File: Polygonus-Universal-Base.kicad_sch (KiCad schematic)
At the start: 6 parts, among them J4 Polygonus_Plugs, J5 Conn_02x04_Top_Bottom, U1 WBO-Single-Module

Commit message: Made the board
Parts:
- removed JP1: Jumper_2_Open, Resistor_THT:R_Axial_DIN0309_L9.0mm_D3.2mm_P15.24mm_Horizontal, symbol Jumper:Jumper_2_Open
- J4: footprint Simon:Polygonus_Plugs -> Simon:Polygonus-With-USB-SWD
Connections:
- net LSU_12v is gone; now on net 12V_MR_FUSE: J5.1 (Pin_1), J5.2 (Pin_2)
- net 12V_KEY: now also Motronic_88pin1.21
- net 12V_MR: now also Motronic_88pin1.10, Motronic_88pin1.28, Motronic_88pin1.37, Motronic_88pin1.68
- net 12V_MR_FUSE: no longer Motronic_88pin1.28
- net 5V_SENSOR_1: now also Motronic_88pin1.58, Motronic_88pin1.59
- net 5V_SENSOR_2: now also Motronic_88pin1.56, Motronic_88pin1.57
- net AT1: now also Motronic_88pin1.15
- net AT2: now also Motronic_88pin1.73
- net AT3: now also Motronic_88pin1.43
- net AT4: now also Motronic_88pin1.16
- net AV1: now also Motronic_88pin1.38
- net AV10: now also Motronic_88pin1.72
- net AV11: now also Motronic_88pin1.14
- net AV2: now also Motronic_88pin1.11
- net AV3: now also Motronic_88pin1.69
- net AV4: now also Motronic_88pin1.39
- net AV5: now also Motronic_88pin1.12
- net AV6: now also Motronic_88pin1.70
- net AV7: now also Motronic_88pin1.40
- net AV8: now also Motronic_88pin1.13
- net AV9: now also Motronic_88pin1.71
- net CAN+: now also Motronic_88pin1.75
- net CAN-: now also Motronic_88pin1.74
- net CRANK +: now also Motronic_88pin1.41
- net CRANK -: now also Motronic_88pin1.42
- net DIGITAL_1: now also Motronic_88pin1.65
- net DIGITAL_2: now also Motronic_88pin1.64
- net DIGITAL_3: now also Motronic_88pin1.63
- net DIGITAL_4: now also Motronic_88pin1.62
- net DIGITAL_5: now also Motronic_88pin1.61
- net DIGITAL_6: now also Motronic_88pin1.60
- net ETB1_+: now also Motronic_88pin1.34
- net ETB1_-: now also Motronic_88pin1.6
- net ETB2_+: now also Motronic_88pin1.33
- net ETB2_-: now also Motronic_88pin1.5
- net ExtraLSA: now also Motronic_88pin1.1
- net ExtraLSB: now also Motronic_88pin1.29
- net ExtraLSC: now also Motronic_88pin1.2
- net ExtraLSD: now also Motronic_88pin1.30
- net GND: now also Motronic_88pin1.55
- net HS1: now also Motronic_88pin1.32
- net HS2: now also Motronic_88pin1.4
- net HS3: now also Motronic_88pin1.31
- net HS4: now also Motronic_88pin1.3
- net IGBT1: now also Motronic_88pin1.25
- net IGBT2: now also Motronic_88pin1.52
- net IGBT3: now also Motronic_88pin1.24
- net IGBT4: now also Motronic_88pin1.51
- net IGBT5: now also Motronic_88pin1.23
- net IGBT6: now also Motronic_88pin1.50
- net IGBT7: now also Motronic_88pin1.22
- net IGBT8: now also Motronic_88pin1.49
- net KNOCK_1: now also Motronic_88pin1.35
- net KNOCK_2: now also Motronic_88pin1.7
- net LS1: now also Motronic_88pin1.76
- net LS10ADD: now also Motronic_88pin1.26
- net LS11ADD: now also Motronic_88pin1.54
- net LS12ADD: now also Motronic_88pin1.27
- net LS13: now also Motronic_88pin1.88
- net LS14: now also Motronic_88pin1.87
- net LS15: now also Motronic_88pin1.86
- net LS16: now also Motronic_88pin1.85
- net LS2: now also Motronic_88pin1.77
- net LS3: now also Motronic_88pin1.78
- net LS4: now also Motronic_88pin1.79
- net LS5: now also Motronic_88pin1.80
- net LS6: now also Motronic_88pin1.81
- net LS7: now also Motronic_88pin1.82
- net LS8: now also Motronic_88pin1.83
- net LS9ADD: now also Motronic_88pin1.53
- net Perm_Live: now also Motronic_88pin1.84

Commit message: Competed board
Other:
- note removed: "1 Fuel pump 2 ICV close 3 inj 1 4 inj 4 5 inj 6 6 GND injection 7 inj 7 8 check engine 9 10 11 transmisson TPS 12 HEGO signal 13 HEGO signal 14 MAF ground 15 Injection signal resistor? 16 CPS pos 17 Cam sensor 18 19 Secondary air pump 20 21 22 IGN 7 23 IGN 6 24 IGN 4 25 IGN 1 26 12v B+junction 27 Main relay 28 GND shields and sensors"
- note removed: "1 Fuel pump 2 ICV close 3 inj 5 4 inj 6 5 inj 4 6 GND injection 7 vanos 8 check engine 9 10 11 transmisson TPS 12 13 HEGO signal 14 MAF ground 15 GND via resistor? 16 CPS pos 17 Cam sensor 18 19 20 21 22 23 IGN 4 24 IGN 6 25 IGN 5 26 12v B+junction 27 Main relay 28 GND shields and sensors"
- note removed: "29 ICV open 30 31 inj 3 32 inj 2 33 inj 1 34 GND 35 36 EVAP 37 38 HEGO heater 39 40 HEGO signal gnd 41 MAF 42 VSS 43 CPS neg 44 GND sensors 45 GND shields 46 TI fuel 47 Tacho 48 AC control 49 50 ign 1 51 ign 2 52 ign 3 53 54 Main relay voltage 55 GND ignition"
- note removed: "29 ICV open 30 31 inj 3 32 inj 2 33 inj 1 34 GND 35 inj 2 36 EVAP 37 HEGO heater 38 39 HEGO signal gnd 40 HEGO signal gnd 41 MAF signal 42 VSS 43 CPS neg 44 GND sensors 45 GND shields 46 TI fuel 47 Tacho 48 AC control 49 IGN 2 50 IGN 3 51 IGN 8 52 IGN 5 53 54 Main relay voltage 55 GND ignition"
- note removed: "56 12v key 57 58 59 5v sensor 60 data link 61 62 EML abs/asc 63 64 AC switch 65 AC pressure 66 EWSII 67 Knock 68 Knock 69 Knock 70 Knock 71 GND knock sensor 72 73 TPS 74 75 76 77 IAT 78 ECT 79 80 81 Headlights on signal 82 Engine overrun signal ABS/ASC 83 traction regulation ABS/ASC 84 GND 85 TCU data 86 TCU data 87 RxD 88 TxD"
- note removed: "56 12v key 57 Transmission IGN RET 58 59 5v sensor 60 data link 61 62 EML abs/asc 63 64 AC switch 65 AC pressure 66 EWSII 67 68 69 Knock 70 Knock 71 GND knock sensor 72 73 TPS 74 75 76 77 IAT 78 ECT 79 80 81 Trans range switch 82 Throttle ABS/ASC 83 Ignition ABS/ASC 84 85 86 87 RxD 88 TxD"
- note removed: "Large Pins 1 to 6 22 to 28 29 to 34 49 to 55"
- moved on the sheet: F1, J4, J5, Motronic_88pin1A, U1

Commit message: upgraded
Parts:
- added C10: 1u, Resistor_SMD:R_0805_2012Metric, symbol hellen-one-common:Res
- added C11: 56u, Capacitor_THT:CP_Radial_D8.0mm_P3.50mm, symbol Device:CP
- added J1: Conn_02x04_Top_Bottom, Connector_Molex:Molex_Micro-Fit_3.0_43045-0800_2x04_P3.00mm_Horizontal, symbol Connector_Generic:Conn_02x04_Top_Bottom
- added R13, R14: DNP, Resistor_SMD:R_0805_2012Metric, symbol hellen-one-common:Res
- added U14: WBO-Single-Module, wideband_module:f042_wideband_module, symbol Simon:WBO-Single-Module
- J4: footprint Simon:Polygonus-With-USB-SWD -> Simon:Polygonus_Plugs; symbol Simon:Polygonus_Plugs -> Simon:Polygonus-With-USB-SWD
- U1: footprint Simon:f042_wideband_module -> wideband_module:f042_wideband_module
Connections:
- net +5V: now also U14.1 (5v_in)
- net 12V_MR: no longer Motronic_88pin1.10, Motronic_88pin1.37, Motronic_88pin1.68
- net 12V_MR_FUSE: now also Motronic_88pin1.10, Motronic_88pin1.37, Motronic_88pin1.68, C11.1, J1.1 (Pin_1), J1.2 (Pin_2)
- net 5V_SENSOR_1: no longer J4.39 (Pin_39)
- net 5V_SENSOR_2: no longer J4.38 (Pin_38)
- net CAN2+: no longer U1.5 (CANRX)
- net CAN2-: no longer U1.6 (CANTX)
- net GND: now also C10.2, C11.2, U14.10 (GND), U14.2 (GND), U14.3 (Select1), U14.9 (GND)
- net RC1: now reaches J4.75 (Pin_75)
- net RC1: now also R13.2
- net RC2: now reaches J4.76 (Pin_76)
- net RC2: now also R14.2
- new net: C10.1, R13.1, R14.1
- new net CAN_RX: U1.5 (CANRX)
- new net CAN_RX2: U14.5 (CANRX)
- new net CAN_TX: U1.6 (CANTX)
- new net CAN_TX2: U14.6 (CANTX)
- new net HeaterNeg2: J1.5 (Pin_5), J1.6 (Pin_6), U14.11 (HeaterNeg), U14.12 (HeaterNeg)
- new net LSU_Ip2: J1.3 (Pin_3), U14.13 (LSU_Ip)
- new net LSU_Rtrim2: J1.8 (Pin_8), U14.15 (LSU_Rtrim)
- new net LSU_Un2: J1.4 (Pin_4), U14.16 (LSU_Un)
- new net LSU_Vm2: J1.7 (Pin_7), U14.14 (LSU_Vm)
- no-connect marks 8 -> 11
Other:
- added sheet WBO-CAN-TRANS (wbo-can-trans.kicad_sch)
- added sheet WBO-CAN-TRANS1 (wbo-can-trans.kicad_sch)

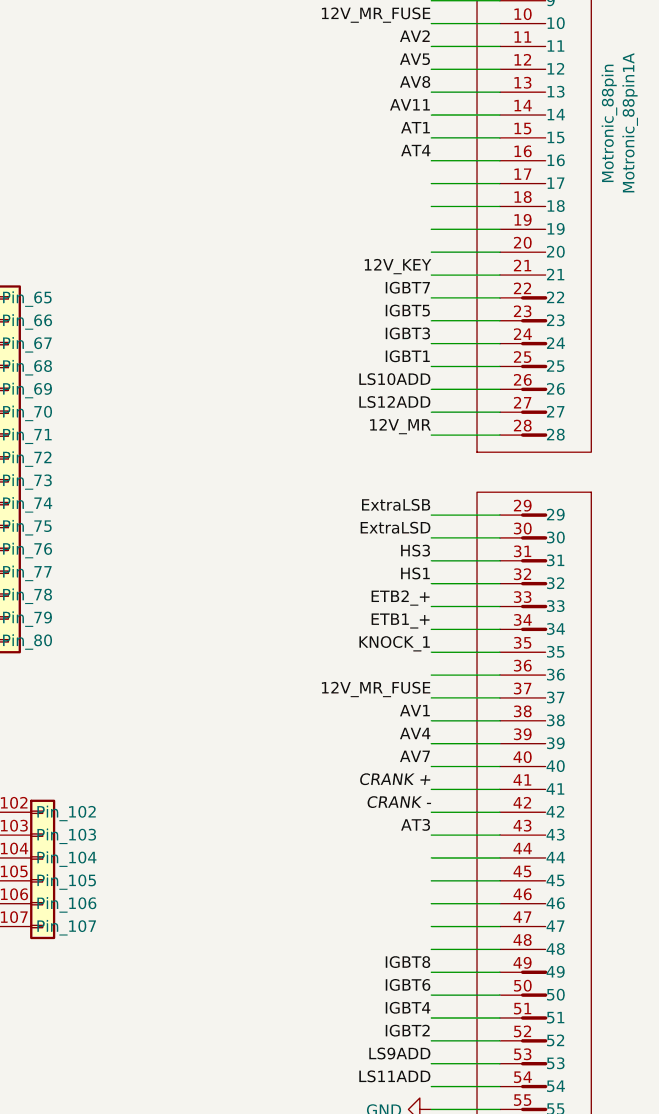
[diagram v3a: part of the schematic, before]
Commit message: Modified IGBTs and routed smart coils
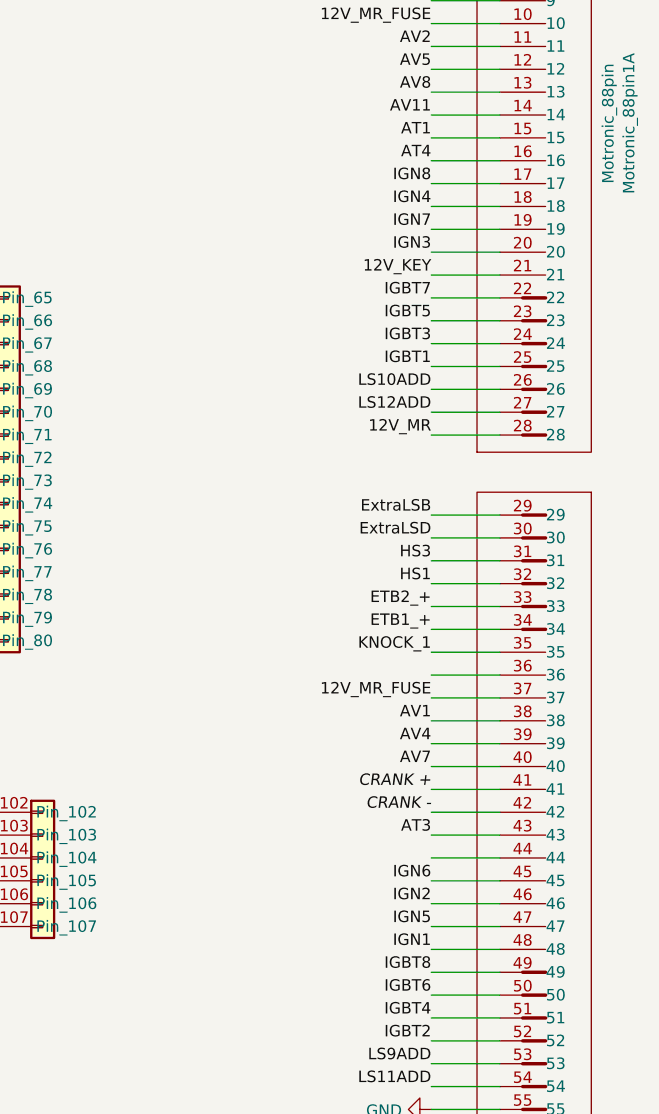
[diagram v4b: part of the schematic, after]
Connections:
- net IGN1: now also Motronic_88pin1.48
- net IGN2: now also Motronic_88pin1.46
- net IGN3: now also Motronic_88pin1.20
- net IGN4: now also Motronic_88pin1.18
- net IGN5: now also Motronic_88pin1.47
- net IGN6: now also Motronic_88pin1.45
- net IGN7: now also Motronic_88pin1.19
- net IGN8: now also Motronic_88pin1.17
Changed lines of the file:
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@@
+    (effects (font (size 1.27 1.27)) (justify right bottom))
+  )
+  (label "IGN4" (at 271.78 73.66 180)
     (effects (font (size 1.27 1.27)) (justify right bottom))
   )
@@
     (effects (font (size 1.27 1.27)) (justify right bottom))
   )
+  (label "IGN6" (at 271.78 148.59 180)
+    (effects (font (size 1.27 1.27)) (justify right bottom))
+  )
   (label "5V_SENSOR_2" (at 271.78 181.61 180)
     (effects (font (size 1.27 1.27)) (justify right bottom))
@@
   )
   (label "12V_MR_FUSE" (at 271.78 53.34 180)
+    (effects (font (size 1.27 1.27)) (justify right bottom))
+  )
+  (label "IGN1" (at 271.78 156.21 180)
     (effects (font (size 1.27 1.27)) (justify right bottom))
   )
@@
     (effects (font (size 1.27 1.27)) (justify right bottom))
   )
+  (label "IGN3" (at 271.78 78.74 180)
+    (effects (font (size 1.27 1.27)) (justify right bottom))
+  )
   (label "12V_MR_FUSE" (at 153.0898 220.274 0)
     (effects (font (size 1.27 1.27)) (justify left bottom))
@@
     (effects (font (size 1.27 1.27)) (justify right bottom))
   )
+  (label "IGN8" (at 271.78 71.12 180)
+    (effects (font (size 1.27 1.27)) (justify right bottom))
+  )
   (label "KNOCK_1" (at 168.91 161.29 180)
     (effects (font (size 1.27 1.27)) (justify right bottom))
@@
     (effects (font (size 1.27 1.27)) (justify right bottom))
   )
+  (label "IGN2" (at 271.78 151.13 180)
+    (effects (font (size 1.27 1.27)) (justify right bottom))
+  )
   (label "AV7" (at 168.91 143.51 180)
     (effects (font (size 1.27 1.27)) (justify right bottom))
@@
     (effects (font (size 1.27 1.27)) (justify right bottom))
   )
+  (label "IGN5" (at 271.78 153.67 180)
+    (effects (font (size 1.27 1.27)) (justify right bottom))
+  )
   (label "IGN7" (at 149.86 46.99 180)
     (effects (font (size 1.27 1.27)) (justify right bottom))
@@
     (effects (font (size 1.27 1.27)) (justify right bottom))
   )
+  (label "IGN7" (at 271.78 76.2 180)
+    (effects (font (size 1.27 1.27)) (justify right bottom))
+  )

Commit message: updated and fixed, check JLC exports
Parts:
- J4: footprint Simon:Polygonus_Plugs -> Simon:Polygonus-With-USB-SWD
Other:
- moved on the sheet: C10, C11, F1, J1, J5, R13, R14, U1, U14

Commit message: All fixed up for JLC
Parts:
- C10, R13, R14: LCSC C23241 -> DNP
- F1: LCSC (none) -> C5249699
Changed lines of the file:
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@@
       (effects (font (size 1.27 1.27)) hide)
     )
-    (property "LCSC" "C23241" (id 4) (at 219.71 186.69 0)
+    (property "LCSC" "DNP" (id 4) (at 219.71 186.69 0)
       (effects (font (size 1.27 1.27)) hide)
     )
@@
       (effects (font (size 1.27 1.27)) hide)
     )
-    (property "LCSC" "C23241" (id 4) (at 219.71 193.04 0)
+    (property "LCSC" "DNP" (id 4) (at 219.71 193.04 0)
       (effects (font (size 1.27 1.27)) hide)
     )
@@
       (effects (font (size 1.27 1.27)) hide)
     )
+    (property "LCSC" "C5249699" (id 4) (at 170.18 184.15 90)
+      (effects (font (size 1.27 1.27)) hide)
+    )
     (pin "1")
     (pin "2")
@@
       (effects (font (size 1.27 1.27)) hide)
     )
-    (property "LCSC" "C23241" (id 4) (at 219.71 193.04 0)
-      (effects (font (size 1.27 1.27)) hide)
-    )
+    (property "LCSC" "DNP" (id 4) (at 219.71 193.04 0)
+      (effects (font (size 1.27 1.27)) hide)
+    )
